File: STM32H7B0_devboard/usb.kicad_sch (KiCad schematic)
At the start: 4 parts, among them J3 USB-C 16P, U5 USBLC6-2SC6

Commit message: Started on V2
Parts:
- removed FL1: TDK ACM2012-900, ACM2012_900_2P_T002:ACM2012_TDK, symbol Filter:Choke_Coilcraft_0603USB-222
- removed J3: USB-C 16P, Connector_USB:USB_C_Receptacle_HCTL_HC-TYPE-C-16P-01A, symbol Connector:USB_C_Receptacle_USB2.0_16P
- removed R22: 5k1, Resistor_SMD:R_0603_1608Metric, symbol Device:R_Small
- removed U5: USBLC6-2SC6, Package_TO_SOT_SMD:SOT-23-6, symbol Power_Protection:USBLC6-2SC6
- added J1: USB-C, symbol Connector:USB_C_Receptacle_USB2.0_16P
- added R1: 5k1, Resistor_SMD:R_0603_1608Metric, symbol Device:R_Small
- added U3: USBLC6-2SC6, Package_TO_SOT_SMD:SOT-23-6, symbol Power_Protection:USBLC6-2SC6
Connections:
- net GND: now also J1.A1 (GND), J1.A12 (GND), J1.B1 (GND), J1.B12 (GND), R1.1, U3.2 (GND)
- net USB_DN: now also U3.6 (I/O1)
- net USB_DP: now also U3.4 (I/O2)
- new net: J1.A5 (CC1), J1.B5 (CC2), R1.2
- new net: J1.A6 (D+), J1.B6 (D+), U3.3 (I/O2)
- new net: J1.A7 (D-), J1.B7 (D-), U3.1 (I/O1)
- new net +5V: J1.A4 (VBUS), J1.A9 (VBUS), J1.B4 (VBUS), J1.B9 (VBUS), U3.5 (VBUS)
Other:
- note removed: "CC1"
- note removed: "CC2"
- note removed: "OUT"
- note removed: "USB_DN"
- note removed: "USB_DP"
- note removed: "VBUS"

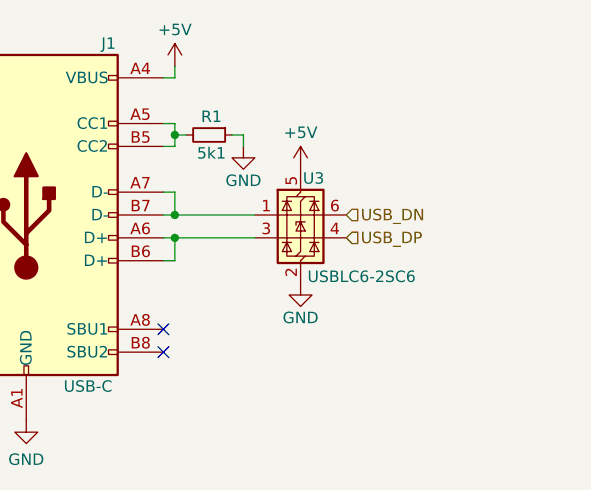
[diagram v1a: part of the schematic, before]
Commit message: Upgraded QSPI flash
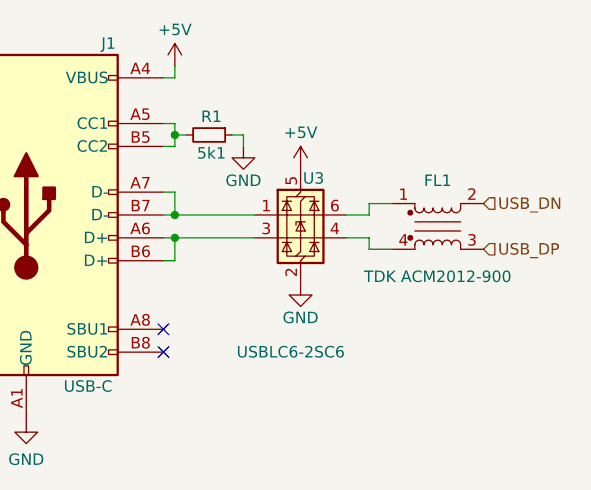
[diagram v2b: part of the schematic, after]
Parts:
- added FL1: TDK ACM2012-900, ACM2012_900_2P_T002:ACM2012_TDK, symbol Filter:Choke_Coilcraft_0603USB-222
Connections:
- net USB_DN: now also FL1.2; no longer U3.6 (I/O1)
- net USB_DP: now also FL1.3; no longer U3.4 (I/O2)
- new net: FL1.1, U3.6 (I/O1)
- new net: FL1.4, U3.4 (I/O2)
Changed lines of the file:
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@@
+	(wire
+		(pts
+			(xy 72.39 45.72) (xy 74.93 45.72)
+		)
+		(stroke
+			(width 0)
+			(type default)
+		)
+	)
+	(wire
+		(pts
+			(xy 74.93 46.99) (xy 74.93 45.72)
+		)
+		(stroke
+			(width 0)
+			(type default)
+		)
+	)
 	(wire
 		(pts
@@
 	(wire
 		(pts
+			(xy 74.93 43.18) (xy 74.93 41.91)
+		)
+		(stroke
+			(width 0)
+			(type default)
+		)
+	)
+	(wire
+		(pts
 			(xy 52.07 33.02) (xy 53.34 33.02)
 		)
@@
 	(wire
 		(pts
+			(xy 74.93 41.91) (xy 77.47 41.91)
+		)
+		(stroke
+			(width 0)
+			(type default)
+		)
+	)
+	(wire
+		(pts
 			(xy 53.34 45.72) (xy 62.23 45.72)
 		)
@@
 	(wire
 		(pts
+			(xy 72.39 43.18) (xy 74.93 43.18)
+		)
+		(stroke
+			(width 0)
+			(type default)
+		)
+	)
+	(wire
+		(pts
 			(xy 52.07 35.56) (xy 53.34 35.56)
 		)
@@
 		(pts
 			(xy 53.34 33.02) (xy 53.34 34.29)
+		)
+		(stroke
+			(width 0)
+			(type default)
+		)
+	)
+	(wire
+		(pts
+			(xy 77.47 46.99) (xy 74.93 46.99)
 		)
 		(stroke
@@
 	(hierarchical_label "USB_DP"
 		(shape input)
-		(at 72.39 45.72 0)
+		(at 87.63 46.99 0)
 		(fields_autoplaced yes)
 		(effects
@@
 	(hierarchical_label "USB_DN"
 		(shape input)
-		(at 72.39 43.18 0)
+		(at 87.63 41.91 0)
 		(fields_autoplaced yes)
 		(effects
@@
 	)
 	(symbol
+		(lib_id "Filter:Choke_Coilcraft_0603USB-222")
+		(at 82.55 44.45 0)
+		(unit 1)
+		(exclude_from_sim no)
+		(in_bom yes)
+		(on_board yes)
+		(dnp no)
+		(property "Reference" "FL1"
+			(at 82.55 39.37 0)
+			(effects
+				(font
+					(size 1.27 1.27)
+				)
+			)
+		)
+		(property "Value" " TDK ACM2012-900"
+			(at 82.55 50.038 0)
+			(effects
+				(font
+					(size 1.27 1.27)
+				)
+			)
+		)
+		(property "Footprint" "ACM2012_900_2P_T002:ACM2012_TDK"
+			(at 82.55 50.8 0)
+			(effects
+				(font
+					(size 1.27 1.27)
+				)
+				(hide yes)
+			)
+		)
+		(property "Datasheet" "https://www.lcsc.com/datasheet/lcsc_datasheet_2304140030_TDK-ACM2012-900-2P-T002_C19972.pdf"
+			(at 82.55 52.705 0)
+			(effects
+				(font
+					(size 1.27 1.27)
+				)
+				(hide yes)
+			)
+		)
+		(property "Description" " TDK ACM2012-900-2P-T002 "
+			(at 82.55 44.45 0)
+			(effects
+				(font
+					(size 1.27 1.27)
+				)
+				(hide yes)
+			)
+		)
+		(property "LCSC" "C19972"
+			(at 82.55 44.45 0)
+			(effects
+				(font
+					(size 1.27 1.27)
+				)
+				(hide yes)
+			)
+		)
+		(pin "1"
+		)
+		(pin "3"
+		)
+		(pin "4"
+		)
+		(pin "2"
+		)
+		(instances
+			(project "STM32H7B0_devboard"
+				(path "/b5cf145c-8a51-4c09-92d2-b17504a94966/6d05f94b-a37c-4021-abab-0c821d29bcc3"
+					(reference "FL1")
+					(unit 1)
+				)
+			)
+		)
+	)
+	(symbol
 		(lib_id "Power_Protection:USBLC6-2SC6")
 		(at 67.31 43.18 0)
@@
 		)
 		(property "Value" "USBLC6-2SC6"
-			(at 68.072 50.038 0)
-			(effects
-				(font
+			(at 60.198 58.42 0)
+			(effects
+				(font

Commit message: Schematic complete
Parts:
- J1: footprint (none) -> Connector_USB:USB_C_Receptacle_G-Switch_GT-USB-7010ASV
- renumbered R1 to R12, U3 to U5
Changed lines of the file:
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@@
 		(on_board yes)
 		(dnp no)
-		(property "Reference" "#PWR06"
+		(property "Reference" "#PWR042"
 			(at 60.96 41.91 0)
 			(effects
@@
 			(project "STM32H7B0_devboard"
 				(path "/b5cf145c-8a51-4c09-92d2-b17504a94966/6d05f94b-a37c-4021-abab-0c821d29bcc3"
-					(reference "#PWR06")
+					(reference "#PWR042")
 					(unit 1)
 				)
@@
 		(on_board yes)
 		(dnp no)
-		(property "Reference" "#PWR08"
+		(property "Reference" "#PWR044"
 			(at 67.31 57.15 0)
 			(effects
@@
 			(project "STM32H7B0_devboard"
 				(path "/b5cf145c-8a51-4c09-92d2-b17504a94966/6d05f94b-a37c-4021-abab-0c821d29bcc3"
-					(reference "#PWR08")
+					(reference "#PWR044")
 					(unit 1)
 				)
@@
 		(on_board yes)
 		(dnp no)
-		(property "Reference" "#PWR07"
+		(property "Reference" "#PWR043"
 			(at 67.31 41.91 0)
 			(effects
@@
 			(project "STM32H7B0_devboard"
 				(path "/b5cf145c-8a51-4c09-92d2-b17504a94966/6d05f94b-a37c-4021-abab-0c821d29bcc3"
-					(reference "#PWR07")
+					(reference "#PWR043")
 					(unit 1)
 				)
@@
 			)
 		)
-		(property "Footprint" ""
+		(property "Footprint" "Connector_USB:USB_C_Receptacle_G-Switch_GT-USB-7010ASV"
 			(at 40.64 43.18 0)
 			(effects
@@
 		(on_board yes)
 		(dnp no)
-		(property "Reference" "#PWR09"
+		(property "Reference" "#PWR045"
 			(at 36.83 72.39 0)
 			(effects
@@
 			(project "STM32H7B0_devboard"
 				(path "/b5cf145c-8a51-4c09-92d2-b17504a94966/6d05f94b-a37c-4021-abab-0c821d29bcc3"
-					(reference "#PWR09")
+					(reference "#PWR045")
 					(unit 1)
 				)
@@
 		(on_board yes)
 		(dnp no)
-		(property "Reference" "R1"
+		(property "Reference" "R12"
 			(at 57.404 32.258 90)
 			(effects
@@
 			(project "STM32H7B0_devboard"
 				(path "/b5cf145c-8a51-4c09-92d2-b17504a94966/6d05f94b-a37c-4021-abab-0c821d29bcc3"
-					(reference "R1")
+					(reference "R12")
 					(unit 1)
 				)
@@
 		(on_board yes)
 		(dnp no)
-		(property "Reference" "#PWR05"
+		(property "Reference" "#PWR041"
 			(at 53.34 30.48 0)
 			(effects
@@
 			(project "STM32H7B0_devboard"
 				(path "/b5cf145c-8a51-4c09-92d2-b17504a94966/6d05f94b-a37c-4021-abab-0c821d29bcc3"
-					(reference "#PWR05")
+					(reference "#PWR041")
 					(unit 1)
 				)
@@
 		(on_board yes)
 		(dnp no)
-		(property "Reference" "U3"
+		(property "Reference" "U5"
 			(at 67.564 39.116 0)
 			(effects
@@
 			(project "STM32H7B0_devboard"
 				(path "/b5cf145c-8a51-4c09-92d2-b17504a94966/6d05f94b-a37c-4021-abab-0c821d29bcc3"
-					(reference "U3")
-					(unit 1)
-				)
+					(reference "U5")
+					(unit 1)
+				)
